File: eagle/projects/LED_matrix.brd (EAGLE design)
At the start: 170 x 100 mm, 142 parts, among them IC1001 7805_T_HORIZONTAL, IC101 4093N, IC102 74LS00, IC103 74193N, IC201 7495N, IC202 74175N, IC301 7495N, IC302 74175N, IC401 7495N, IC402 74175N, IC501 7495N, IC502 74175N, IC901 NE555V, T701 BC548C, T702 BC548C, T703 BC548C, T704 BC548C, T705 BC548C, T706 BC548C, T707 BC548C, T708 BC548C, T709 BC548C, T801 BC548C, T802 BC548C, T803 BC548C, T804 BC548C, T805 BC548C, T806 BC548C, T807 BC548C, T901 BD136, X1001 CLAMP_1X2-T-5MM, X1101 MALE_2X13-T-VERTICAL_2.54MM

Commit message: perpare for release
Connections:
- net N$1 renamed CLK_SLOW_RA
- net N$3 renamed TIM_RA
- net P5V: now also IC102.9
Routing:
- net P5V: track 684.6 -> 688.5 mm

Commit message: changed values for oscillators
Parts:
- C101: value 1u -> 470n
- C102: value 10n -> 1n
- R103: value 1M -> 500k
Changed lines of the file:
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@@
 </autorouter>
 <elements>
-<element name="C102" library="be_rcl" package="T_DISC_4MM_PITCH_5MM" value="10n" x="57" y="8.6" smashed="yes" rot="R180">
+<element name="C102" library="be_rcl" package="T_DISC_4MM_PITCH_5MM" value="1n" x="57" y="8.6" smashed="yes" rot="R180">
 <attribute name="FUNCTION" value="" x="57" y="8.6" size="1.778" layer="27" rot="R180" display="off"/>
 <attribute name="COMMISSIONED" value="2018-12-23" x="57" y="8.6" size="1.778" layer="27" rot="R180" display="off"/>
@@
 <attribute name="VALUE" x="53.2" y="8.4" size="1" layer="27" font="vector" ratio="15" rot="R180"/>
 </element>
-<element name="C101" library="be_rcl" package="T_RADIAL_5MM_GRID_2.54MM" value="1u" x="81.1" y="15.2" smashed="yes" rot="R90">
+<element name="C101" library="be_rcl" package="T_RADIAL_5MM_GRID_2.54MM" value="470n" x="81.1" y="15.2" smashed="yes" rot="R90">
 <attribute name="FUNCTION" value="" x="81.1" y="15.2" size="1.778" layer="27" rot="R90" display="off"/>
 <attribute name="COMMISSIONED" value="2015-01-15" x="81.1" y="15.2" size="1.778" layer="27" rot="R90" display="off"/>
-<attribute name="PART_CODE_BEL" value="C_PAC_T_RADIAL_5mm_PITCH_2mm54_VAL_1u" x="81.1" y="15.2" size="1.778" layer="27" rot="R90" display="off"/>
+<attribute name="PART_CODE_BEL" value="C_PAC_T_RADIAL_5mm_PITCH_2mm54_VAL_470n" x="81.1" y="15.2" size="1.778" layer="27" rot="R90" display="off"/>
 <attribute name="BOM" value="YES" x="81.1" y="15.2" size="1.778" layer="27" rot="R90" display="off"/>
 <attribute name="UPDATED" value="" x="81.1" y="15.2" size="1.778" layer="27" rot="R90" display="off"/>
@@
 <attribute name="VALUE" x="63.3" y="6.2" size="1" layer="27" font="vector" ratio="15" rot="R180"/>
 </element>
-<element name="R103" library="be_rcl" package="T_TRIM_PIHER_PT10_HORIZONTAL" value="1M" x="75.1" y="8.7" smashed="yes" rot="R270">
+<element name="R103" library="be_rcl" package="T_TRIM_PIHER_PT10_HORIZONTAL" value="500k" x="75.1" y="8.7" smashed="yes" rot="R270">
 <attribute name="FUNCTION" value="REFRESH RATE" x="71.2" y="1.8" size="1" layer="27" font="vector" ratio="15"/>
 <attribute name="COMMISSIONED" value="2018-11-11" x="75.1" y="8.7" size="1.778" layer="27" rot="R270" display="off"/>
-<attribute name="PART_CODE_BEL" value="R_PAC_T_TRIM_PIHER_PT10_HORIZONTAL_VAL_" x="75.1" y="8.7" size="1.778" layer="27" rot="R270" display="off"/>
+<attribute name="PART_CODE_BEL" value="R_PAC_T_TRIM_PIHER_PT10_HORIZONTAL_VAL_500k" x="75.1" y="8.7" size="1.778" layer="27" rot="R270" display="off"/>
 <attribute name="BOM" value="YES" x="75.1" y="8.7" size="1.778" layer="27" rot="R270" display="off"/>
 <attribute name="UPDATED" value="" x="75.1" y="8.7" size="1.778" layer="27" rot="R270" display="off"/>

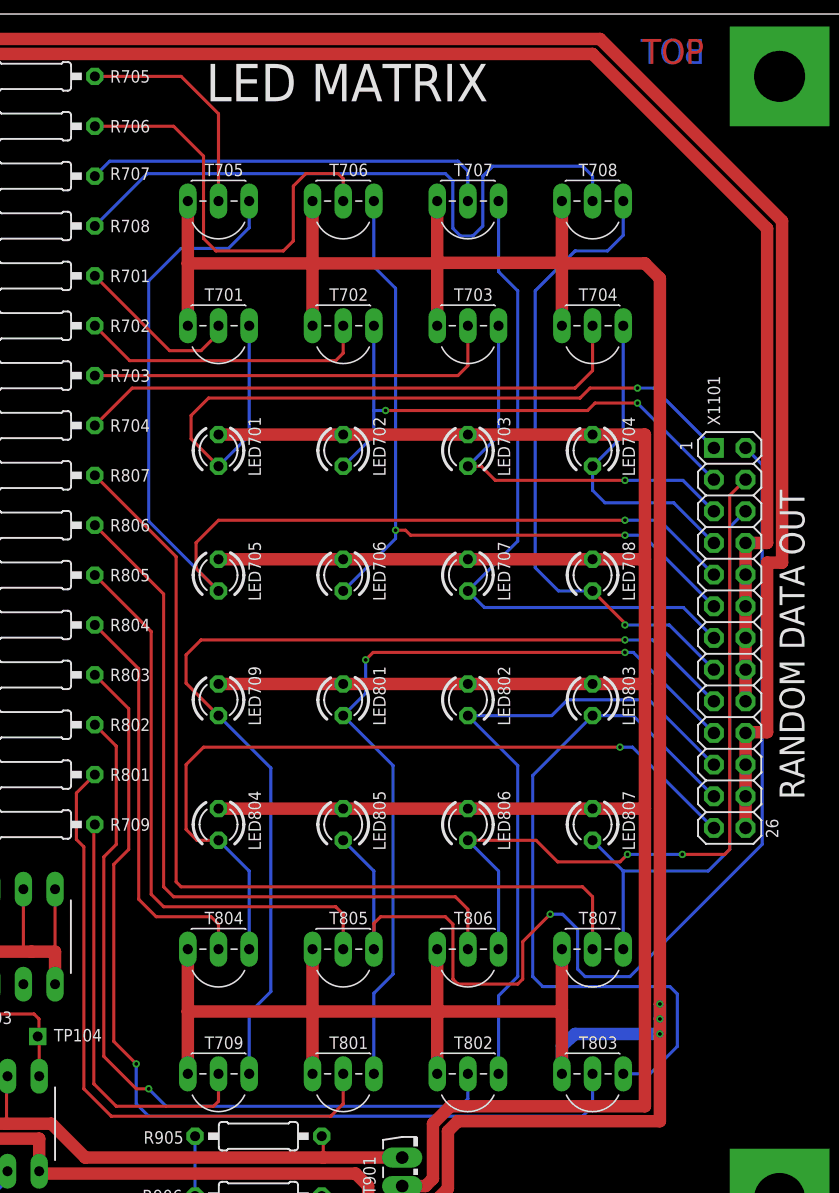
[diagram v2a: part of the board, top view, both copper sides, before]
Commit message: add LED resistors
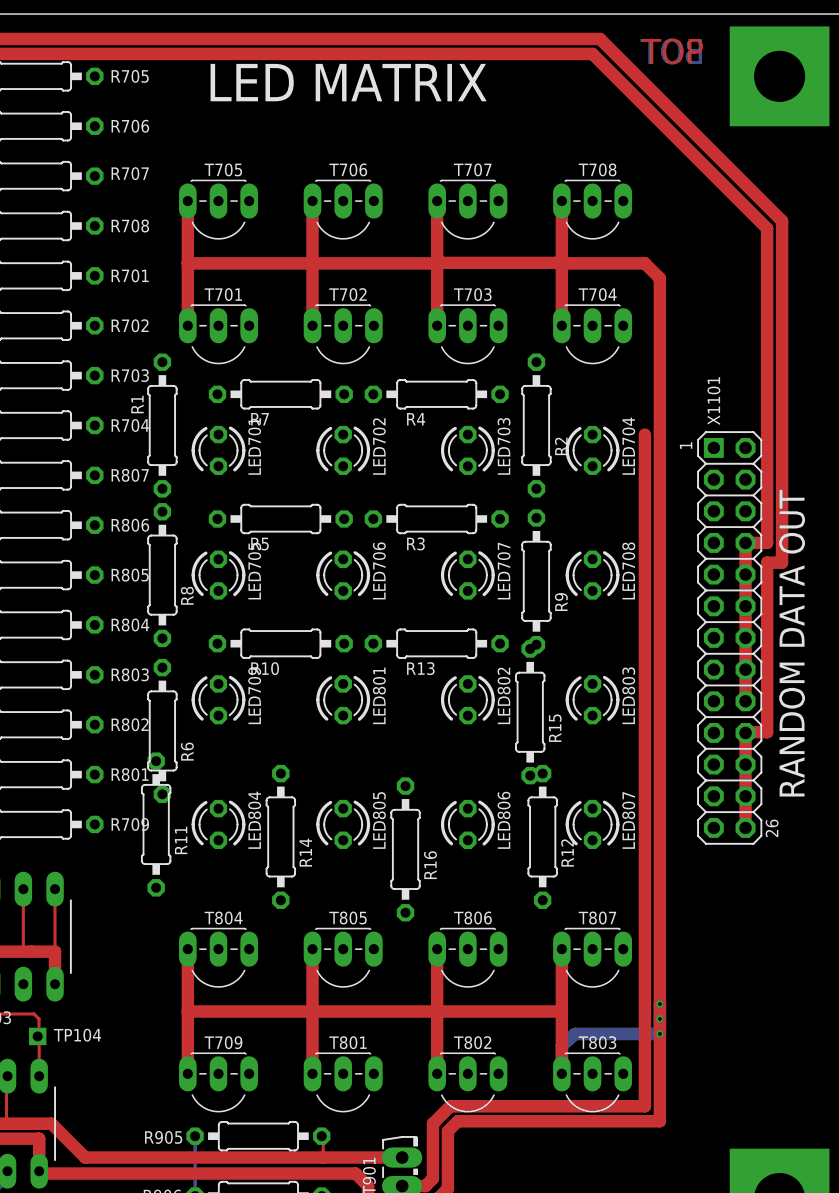
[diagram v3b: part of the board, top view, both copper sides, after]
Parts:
- added R1, R10, R11, R12, R13, R14, R15, R16, R2, R3, R4, R5, R6, R7, R8, R9: 330, be_rcl:T_0207_PITCH_10MM
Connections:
- new net N$1: LED701.A, R1.2
- new net N$10: LED801.A, R10.2
- new net N$11: LED804.A, R11.2
- new net N$12: LED807.A, R12.2
- new net N$13: LED802.A, R13.2
- new net N$14: LED805.A, R14.2
- new net N$15: LED803.A, R15.2
- new net N$16: LED806.A, R16.2
- new net N$2: LED704.A, R2.2
- new net N$3: LED707.A, R3.2
- new net N$4: LED703.A, R4.2
- new net N$5: LED706.A, R5.2
- new net N$6: LED709.A, R6.2
- new net N$7: LED702.A, R7.2
- new net N$8: LED705.A, R8.2
- new net N$9: LED708.A, R9.2
- net V_LED: now also R1.1, R10.1, R11.1, R12.1, R13.1, R14.1, R15.1, R16.1, R2.1, R3.1, R4.1, R5.1, R6.1, R7.1, R8.1, R9.1; no longer LED701.A, LED702.A, LED703.A, LED704.A, LED705.A, LED706.A, LED707.A, LED708.A, LED709.A, LED801.A, LED802.A, LED803.A, LED804.A, LED805.A, LED806.A, LED807.A
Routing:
- net V_LED: track 215.4 -> 78.6 mm
- net DRV_OUT_14: track 92.8 -> 0.00 mm, vias 1 -> 0
- net DRV_OUT_5: track 87.9 -> 0.00 mm, vias 1 -> 0
- net DRV_OUT_9: track 82.0 -> 0.00 mm, vias 1 -> 0
- net DRV_IN_B12: track 76.7 -> 0.00 mm, vias 1 -> 0
- net DRV_IN_B16: track 73.4 -> 0.00 mm
- net DRV_OUT_10: track 67.1 -> 0.00 mm, vias 2 -> 0
- net DRV_OUT_13: track 63.5 -> 0.00 mm, vias 1 -> 0
- net DRV_OUT_1: track 62.1 -> 0.00 mm, vias 1 -> 0
- net DRV_OUT_15: track 62.1 -> 0.00 mm, vias 2 -> 0
- net DRV_OUT_6: track 61.8 -> 0.00 mm, vias 2 -> 0
- net DRV_IN_B11: track 60.8 -> 0.00 mm, vias 1 -> 0
- net DRV_IN_B15: track 59.6 -> 0.00 mm
- net DRV_OUT_12: track 57.0 -> 0.00 mm
- net DRV_OUT_7: track 54.9 -> 0.00 mm
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
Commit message: route vled
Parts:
- moved R9 22.3 mm to (158.0, 73.0), turned to 270 degrees
- moved R8 18.1 mm to (117.0, 73.0), turned to 270 degrees
- moved R5 15.7 mm to (133.0, 73.0), turned to 270 degrees
- moved R3 13.5 mm to (137.0, 73.0), turned to 270 degrees
- moved R6 12.5 mm to (116.0, 55.0), turned to 270 degrees
- moved R15 11.0 mm to (146.0, 55.0), turned to 270 degrees
- moved R1 9.60 mm to (123.0, 73.0)
- moved T701 7.00 mm to (120.0, 82.0)
- moved T702 7.00 mm to (130.0, 82.0)
- moved T703 7.00 mm to (140.0, 82.0)
- moved T704 7.00 mm to (150.0, 82.0)
- moved R4 6.52 mm to (143.0, 73.0), turned to 270 degrees
- moved R2 6.18 mm to (147.0, 73.0), turned to 270 degrees
- moved R13 5.70 mm to (136.0, 55.0), turned to 270 degrees
- moved R10 5.59 mm to (126.0, 55.0), turned to 270 degrees
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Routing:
- net V_LED: track 78.6 -> 208.1 mm, vias 0 -> 1
- net DRV_IN_B16: track 0.00 -> 84.3 mm
- net DRV_OUT_5: track 0.00 -> 84.1 mm, vias 0 -> 1
- net DRV_IN_B12: track 0.00 -> 78.8 mm, vias 0 -> 1
- net DRV_OUT_14: track 0.00 -> 74.5 mm, vias 0 -> 3
- net DRV_OUT_6: track 0.00 -> 74.4 mm, vias 0 -> 1
- net DRV_OUT_9: track 0.00 -> 74.2 mm
- net DRV_OUT_7: track 0.00 -> 73.4 mm
- net DRV_IN_B11: track 0.00 -> 65.8 mm
- net DRV_IN_B15: track 0.00 -> 65.5 mm, vias 0 -> 1
- net DRV_OUT_10: track 0.00 -> 64.5 mm
- net DRV_OUT_1: track 0.00 -> 62.9 mm, vias 0 -> 2
- net DRV_OUT_2: track 0.00 -> 62.5 mm, vias 0 -> 1
- net DRV_OUT_12: track 0.00 -> 57.1 mm
- net DRV_OUT_8: track 0.00 -> 56.5 mm
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
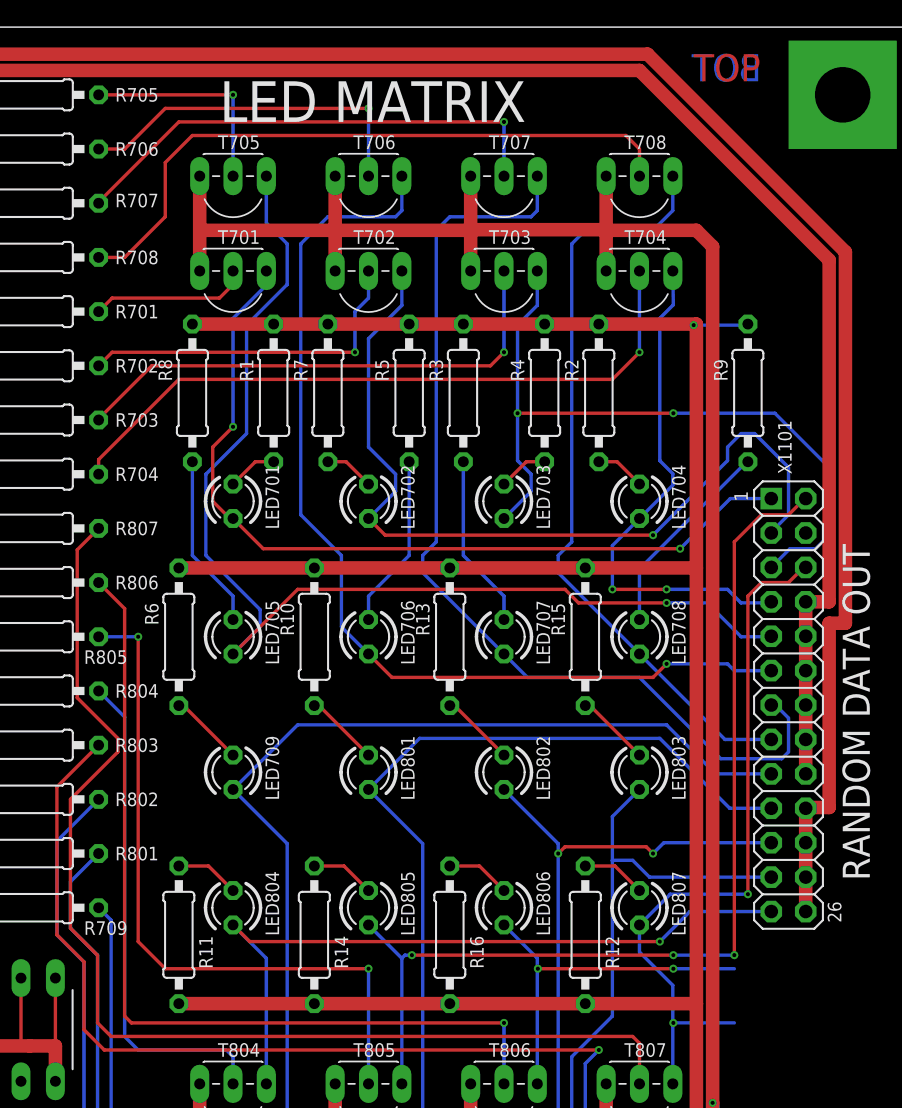
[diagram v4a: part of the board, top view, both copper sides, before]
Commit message: rename anonymous nets
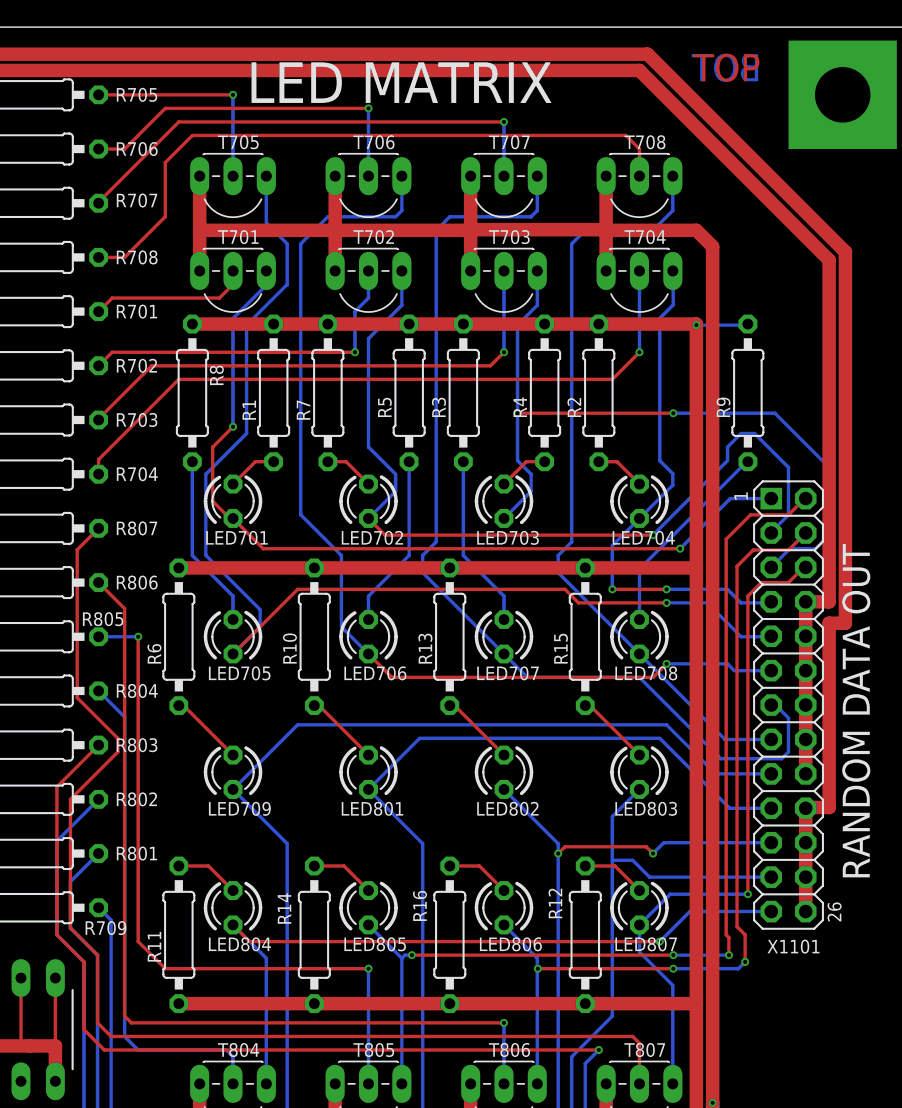
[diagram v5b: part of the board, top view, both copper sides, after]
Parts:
- C101: value 470n -> 1u
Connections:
- net N$1 renamed DRV_OUT_A_1
- net N$10 renamed DRV_OUT_A_10
- net N$11 renamed DRV_OUT_A_13
- net N$12 renamed DRV_OUT_A_16
- net N$13 renamed DRV_OUT_A_11
- net N$14 renamed DRV_OUT_A_14
- net N$15 renamed DRV_OUT_A_12
- net N$16 renamed DRV_OUT_A_15
- net N$2 renamed DRV_OUT_A_4
- net N$3 renamed DRV_OUT_A_7
- net N$4 renamed DRV_OUT_A_3
- net N$5 renamed DRV_OUT_A_6
- net N$6 renamed DRV_OUT_A_9
- net N$7 renamed DRV_OUT_A_2
- net N$8 renamed DRV_OUT_A_5
- net N$9 renamed DRV_OUT_A_8
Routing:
- net DRV_OUT_15: track 27.3 -> 63.8 mm, vias 2 -> 3
- net N$19: track 4.50 -> 0.00 mm, vias 1 -> 0

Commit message: release
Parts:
- removed R1, R10, R13, R15, R4, R7: 330, be_rcl:T_0207_PITCH_10MM
- added R713, R714, R715, R808, R809, R813: 2k7, be_rcl:T_0207_PITCH_10MM
- R704, R705, R706, R804, R805, R806: value 2k7 -> 330
- X1101: value MALE_2X13-T-VERTICAL_2.54MM -> MALE_2X13-T-VERTICAL_PITCH_2MM54; device be_con_jump:T_MALE_2X13_VERTICAL_GRID_2.54MM -> be_con_jump:T_MALE_2X13_VERTICAL_PITCH_2MM54
- moved R709 56.0 mm to (105.0, 91.0)
- moved R706 42.0 mm to (143.0, 73.0), turned to 270 degrees
- moved R806 41.2 mm to (146.0, 55.0), turned to 270 degrees
- moved R705 31.1 mm to (127.0, 73.0), turned to 270 degrees
- moved R805 31.0 mm to (136.0, 55.0), turned to 270 degrees
- moved R804 21.4 mm to (126.0, 55.0), turned to 270 degrees
- moved R707 20.0 mm to (105.0, 67.0)
- moved R704 19.0 mm to (123.0, 73.0), turned to 270 degrees
- moved R708 12.0 mm to (105.0, 95.0)
- moved R807 12.0 mm to (105.0, 51.0)
- renumbered R11 to R810, R12 to R814, R14 to R811, R16 to R812, R2 to R710, R3 to R716, R5 to R712, R6 to R718, R8 to R711, R9 to R717
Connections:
- net DRV_IN_13: now also R807.1; no longer R804.1
- net DRV_IN_14: now also R808.1; no longer R805.1
- net DRV_IN_15: now also R809.1; no longer R806.1
- net DRV_IN_16: now also R813.1; no longer R807.1
- net DRV_IN_4: now also R707.1; no longer R704.1
- net DRV_IN_5: now also R708.1; no longer R705.1
- net DRV_IN_6: now also R709.1; no longer R706.1
- net DRV_IN_7: now also R713.1; no longer R707.1
- net DRV_IN_8: now also R714.1; no longer R708.1
- net DRV_IN_9: now also R715.1; no longer R709.1
- net DRV_IN_B13: now also R807.2; no longer R804.2
- net DRV_IN_B14: now also R808.2; no longer R805.2
- net DRV_IN_B15: now also R809.2; no longer R806.2
- net DRV_IN_B16: now also R813.2; no longer R807.2
- net DRV_IN_B4: now also R707.2; no longer R704.2
- net DRV_IN_B5: now also R708.2; no longer R705.2
- net DRV_IN_B6: now also R709.2; no longer R706.2
- net DRV_IN_B7: now also R713.2; no longer R707.2
- net DRV_IN_B8: now also R714.2; no longer R708.2
- net DRV_IN_B9: now also R715.2; no longer R709.2
- net DRV_OUT_A_1: now also R704.2; no longer R1.2
- net DRV_OUT_A_10: now also R804.2; no longer R10.2
- net DRV_OUT_A_11: now also R805.2; no longer R13.2
- net DRV_OUT_A_12: now also R806.2; no longer R15.2
- net DRV_OUT_A_2: now also R705.2; no longer R7.2
- net DRV_OUT_A_3: now also R706.2; no longer R4.2
- net V_LED: now also R704.1, R705.1, R706.1, R804.1, R805.1, R806.1; no longer R1.1, R10.1, R13.1, R15.1, R4.1, R7.1

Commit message: fix values. add movie
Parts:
- C102: value 1n -> 100n
- R103: value 500k -> 50k
- R901: value 10k -> 1k2
- R902: value 470k -> not fitted
- R905: value 1k -> 10k
- R906: value 1k -> 330
